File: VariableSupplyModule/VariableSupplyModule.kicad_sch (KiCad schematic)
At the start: 10 parts, among them J3 Digital VA measure, J301 Conn_01x03_Socket, Q1 BD139, Q3 TIP2955G, U1 LM317

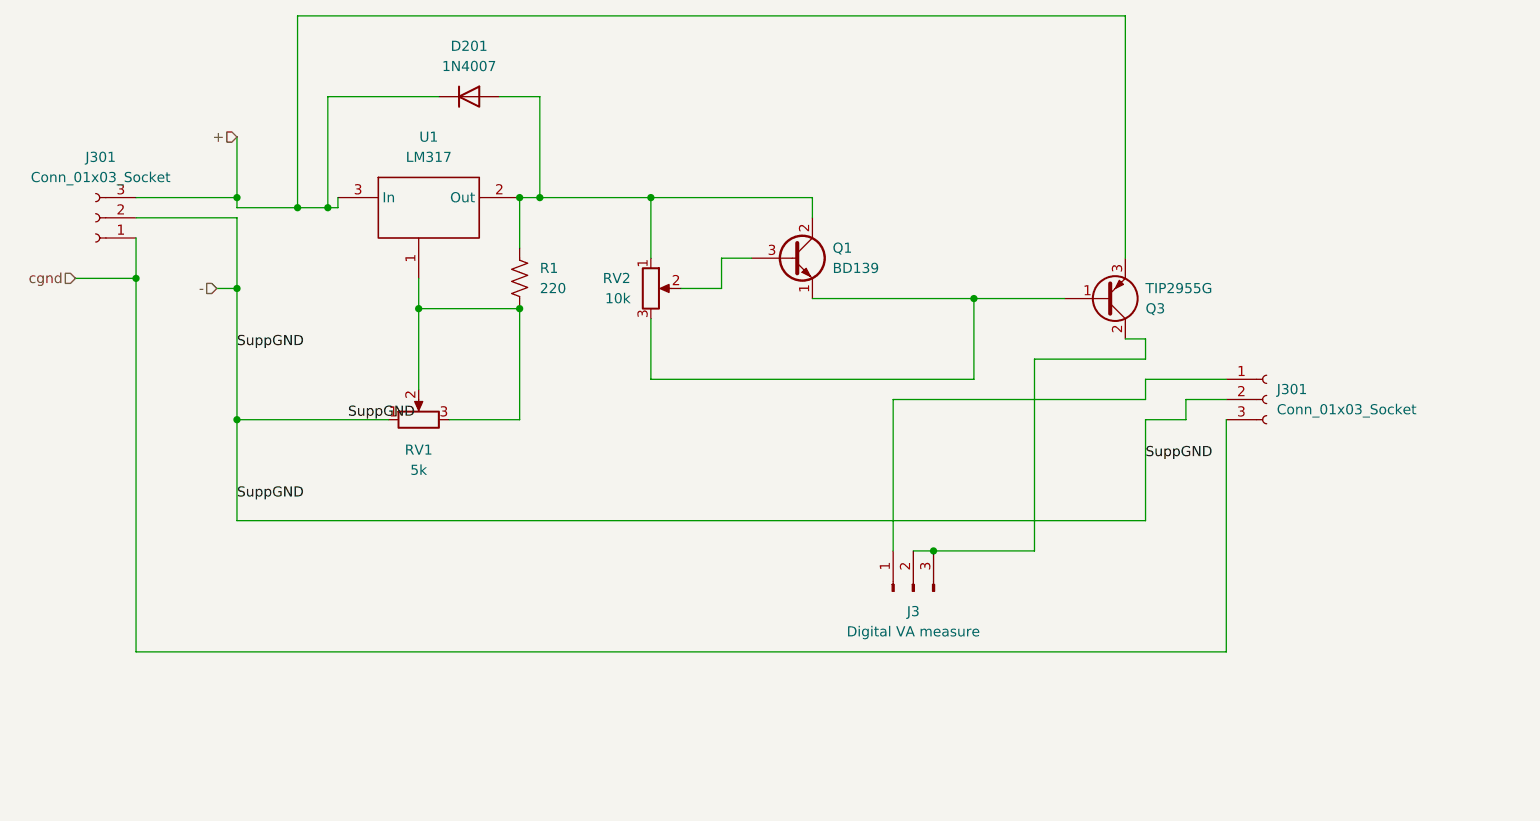
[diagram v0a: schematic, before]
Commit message: Split the design into two separate KiCad projects. 1. The Main Rectifier board with auxilliary 12V supply 2. LM317 Variable Supply module
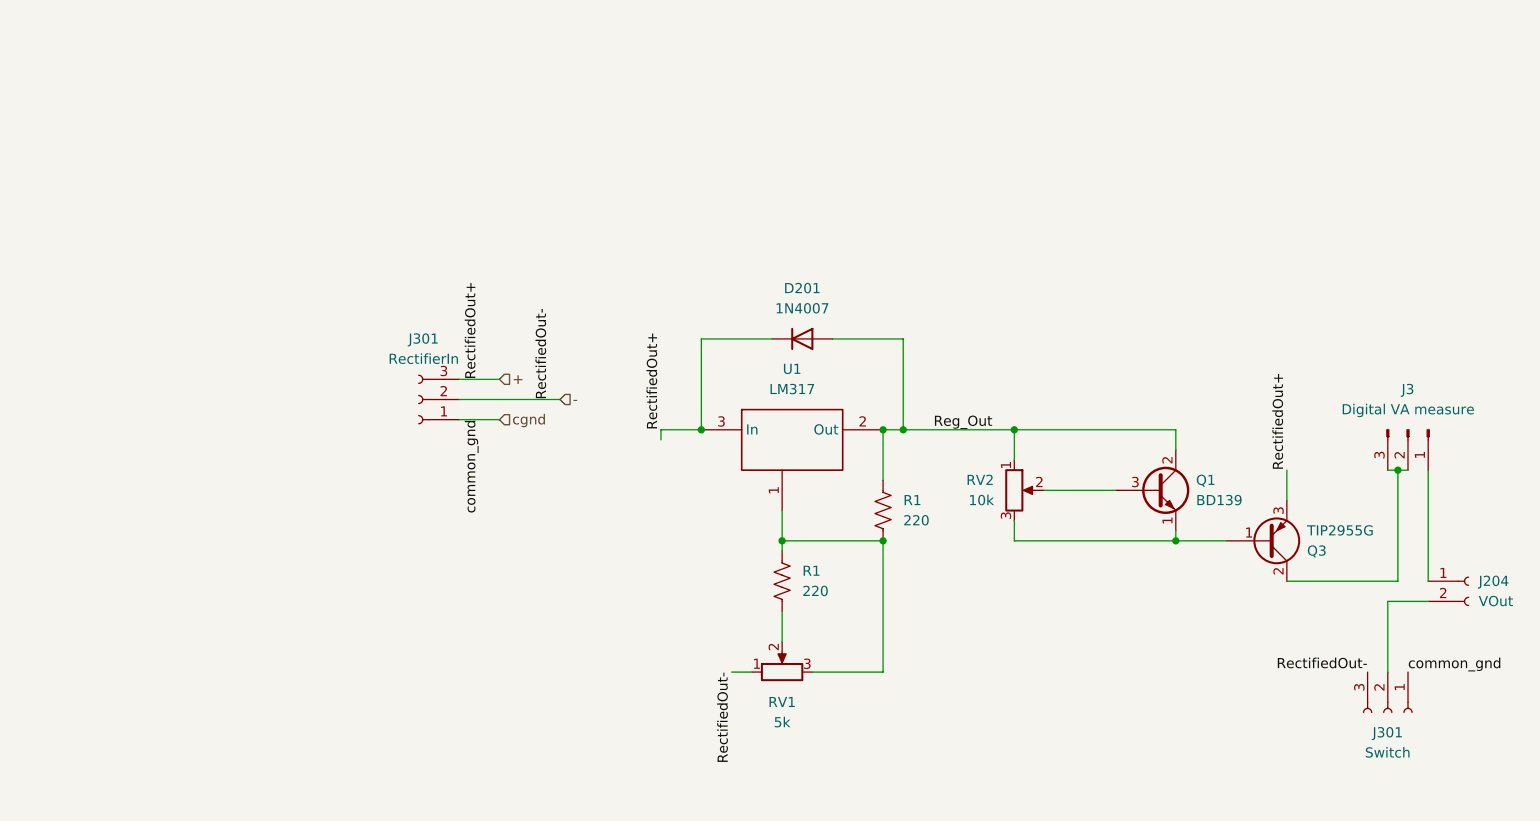
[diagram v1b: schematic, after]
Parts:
- removed J301 (x2): Conn_01x03_Socket, symbol Connector:Conn_01x03_Socket
- removed R1: 220, Resistor_THT:R_Axial_DIN0207_L6.3mm_D2.5mm_P10.16mm_Horizontal, symbol Device:R_US
- added J204: VOut, Connector_JST:JST_VH_B2P-VH_1x02_P3.96mm_Vertical, symbol Connector:Conn_01x02_Socket
- added J301: Switch, Connector_JST:JST_VH_B3P-VH-B_1x03_P3.96mm_Vertical, symbol Connector:Conn_01x03_Socket
- added J301: RectifierIn, Connector_JST:JST_VH_B3P-VH-B_1x03_P3.96mm_Vertical, symbol Connector:Conn_01x03_Socket
- added R1 (x2): 220, Resistor_THT:R_Axial_DIN0207_L6.3mm_D2.5mm_P10.16mm_Horizontal, symbol Device:R_US
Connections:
- net +: now also J301.3 (Pin_3)
- net -: now also J301.2 (Pin_2), J301.3 (Pin_3)
- net cgnd: now also J301.1 (Pin_1), J301.1 (Pin_1)
- net at RV1.3, U1.1: now also R1.1, R1.2; no longer RV1.2
- net Reg_Out: now reaches D201.2 (A), Q1.2 (C), RV2.1, U1.2 (Out)
- net Reg_Out: now also R1.1
- net at J3.1 (Pin_1): now also J204.1 (Pin_1)
- new net: J204.2 (Pin_2), J301.2 (Pin_2)
- new net: R1.2, RV1.2
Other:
- title: Bench power supply -> Variable Supply with LM317
